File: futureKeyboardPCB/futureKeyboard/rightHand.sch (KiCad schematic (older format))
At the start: 50 parts, among them J1 Conn_01x01, J2 Conn_01x04, J3 Conn_01x01, J4 Conn_01x01, J5 Conn_01x04, J6 Conn_01x06, J7 Conn_01x06, J8 Conn_01x01, P1 CONN_01X02, P2 CONN_01X06, Q1 2SC1815, Q2 2SC1815, Q3 2SC1815, SW1 SW_SPDT, SW2 SW_Push, SW3 SW_Push, SW4 SW_Push, SW5 SW_Push, SW6 SW_Push, SW7 SW_Push, SW8 SW_Push, U1 AMS1117-1.5, U2 ESP32

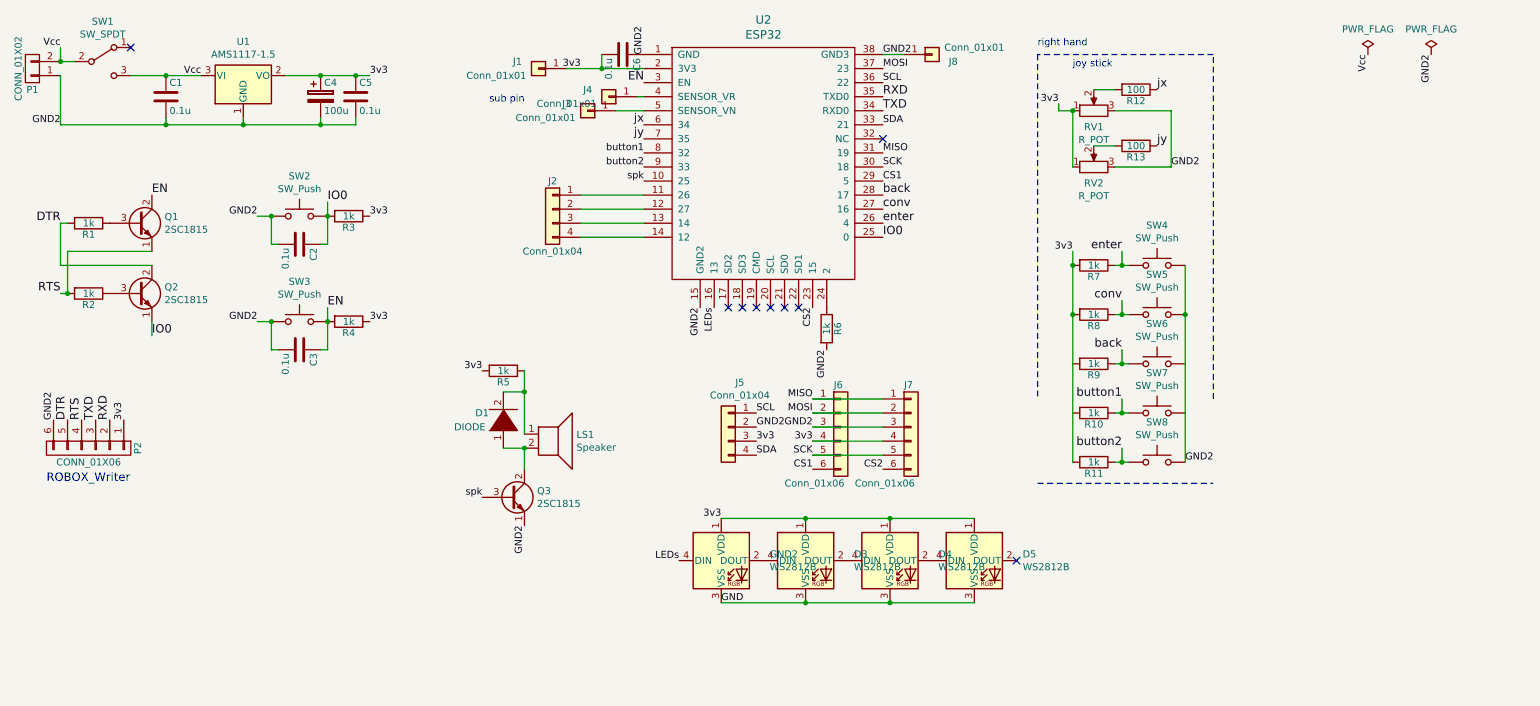
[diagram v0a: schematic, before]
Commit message: divide layors, make footprints, aligned footprints
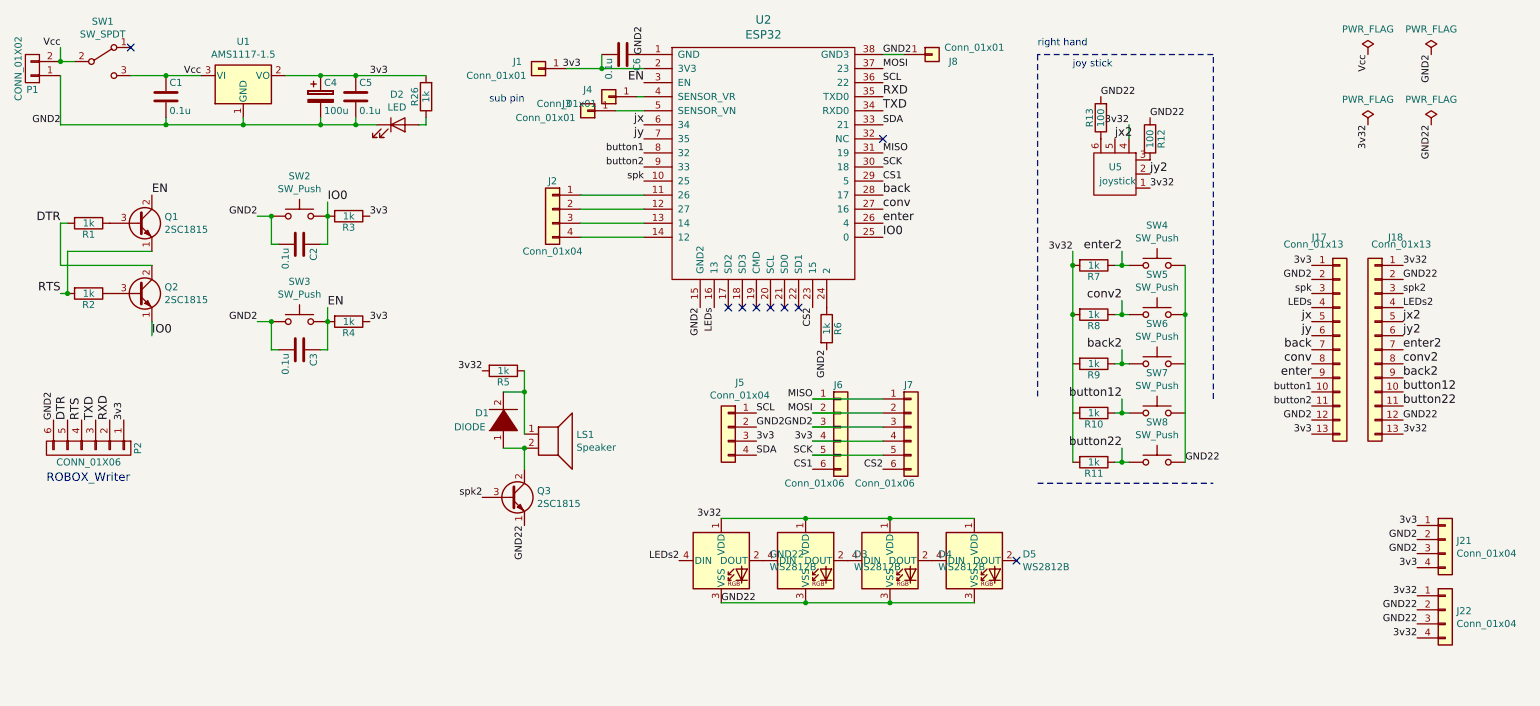
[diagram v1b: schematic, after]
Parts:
- removed RV1, RV2: R_POT, akizukit:S_POT_SMD, symbol Device:R_POT
- added D2: LED, akizukit:2012LED, symbol Device:LED
- added J17, J18: Conn_01x13, Connector_PinHeader_2.54mm:PinHeader_1x13_P2.54mm_Vertical_SMD_Pin1Left, symbol Connector_Generic:Conn_01x13
- added J21, J22: Conn_01x04, Connector_PinHeader_2.54mm:PinHeader_1x04_P2.54mm_Vertical_SMD_Pin1Left, symbol Connector_Generic:Conn_01x04
- added R26: 1k, akizukit:SMD-1608, symbol Hyper_Board_Traser-rescue:R
- added U5: joystick, akizukit:joyStick, symbol akizukit:joystick
- D3, D4, D5: footprint LED_SMD:LED_WS2812B_PLCC4_5.0x5.0mm_P3.2mm -> akizukit:WS2812B
- GND22: renamed from GND2; footprint LED_SMD:LED_WS2812B_PLCC4_5.0x5.0mm_P3.2mm -> akizukit:WS2812B
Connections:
- net GND is gone; now on net GND22: D3.3 (VSS), D4.3 (VSS), D5.3 (VSS), GND22.3 (VSS)
- net 3v3: now also J17.1 (Pin_1), J17.13 (Pin_13), J21.1 (Pin_1), J21.4 (Pin_4), R26.2; no longer D3.1 (VDD), D4.1 (VDD), D5.1 (VDD), GND22.1 (VDD), R10.2, R11.2, R5.2, R7.2, R8.2, R9.2
- net GND2: now also D2.1 (K), J17.12 (Pin_12), J17.2 (Pin_2), J21.2 (Pin_2), J21.3 (Pin_3); no longer Q3.1 (E), SW4.2, SW5.2, SW6.2, SW7.2, SW8.2
- net LEDs: now also J17.4 (Pin_4); no longer GND22.4 (DIN)
- net back: now also J17.7 (Pin_7); no longer R9.1, SW6.1
- net button1: now also J17.10 (Pin_10); no longer R10.1, SW7.1
- net button2: now also J17.11 (Pin_11); no longer R11.1, SW8.1
- net conv: now also J17.8 (Pin_8); no longer R8.1, SW5.1
- net enter: now also J17.9 (Pin_9); no longer R7.1, SW4.1
- net jx: now also J17.5 (Pin_5); no longer R12.1
- net jy: now also J17.6 (Pin_6); no longer R13.1
- net spk: now also J17.3 (Pin_3); no longer Q3.3 (B)
- net GND22: now reaches R13.2
- net GND22: now also Q3.1 (E), R12.1, SW4.2, SW5.2, SW6.2, SW7.2, SW8.2, J18.12 (Pin_12), J18.2 (Pin_2), J22.2 (Pin_2), J22.3 (Pin_3)
- net at R12.2: now also U5.3
- new net: R13.1, U5.6
- new net: D2.2 (A), R26.1
- new net 3v32: D3.1 (VDD), D4.1 (VDD), D5.1 (VDD), GND22.1 (VDD), J18.1 (Pin_1), J18.13 (Pin_13), J22.1 (Pin_1), J22.4 (Pin_4), R10.2, R11.2, R5.2, R7.2, R8.2, R9.2, U5.1, U5.4
- new net LEDs2: GND22.4 (DIN), J18.4 (Pin_4)
- new net back2: J18.9 (Pin_9), R9.1, SW6.1
- new net button12: J18.10 (Pin_10), R10.1, SW7.1
- new net button22: J18.11 (Pin_11), R11.1, SW8.1
- new net conv2: J18.8 (Pin_8), R8.1, SW5.1
- new net enter2: J18.7 (Pin_7), R7.1, SW4.1
- new net jx2: J18.5 (Pin_5), U5.5
- new net jy2: J18.6 (Pin_6), U5.2
- new net spk2: J18.3 (Pin_3), Q3.3 (B)
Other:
- moved on the sheet: R12

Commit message: change layer connecter to be same pins total
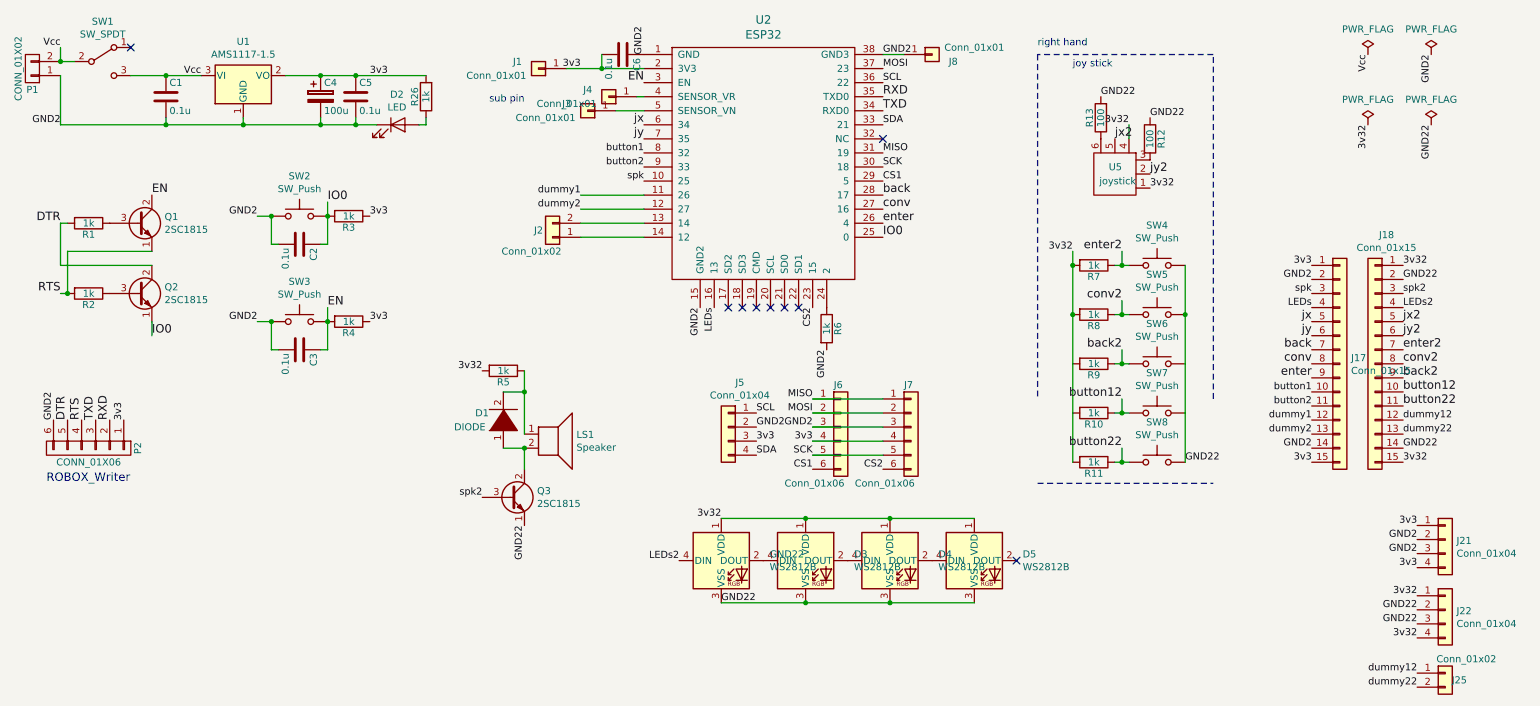
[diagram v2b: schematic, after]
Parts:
- removed J17, J18: Conn_01x13, Connector_PinHeader_2.54mm:PinHeader_1x13_P2.54mm_Vertical_SMD_Pin1Left, symbol Connector_Generic:Conn_01x13
- removed J2: Conn_01x04, Connector_PinHeader_2.54mm:PinHeader_1x04_P2.54mm_Vertical, symbol Connector_Generic:Conn_01x04
- added J17, J18: Conn_01x15, Connector_PinHeader_2.54mm:PinHeader_1x15_P2.54mm_Vertical_SMD_Pin1Left, symbol Connector_Generic:Conn_01x15
- added J2, J25: Conn_01x02, Connector_PinHeader_2.54mm:PinHeader_1x02_P2.54mm_Vertical, symbol Connector_Generic:Conn_01x02
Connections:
- net 3v3: now also J17.1 (Pin_1), J17.15 (Pin_15)
- net 3v32: now also J18.1 (Pin_1), J18.15 (Pin_15)
- net GND2: now also J17.14 (Pin_14), J17.2 (Pin_2)
- net GND22: now also J18.14 (Pin_14), J18.2 (Pin_2)
- net LEDs: now also J17.4 (Pin_4)
- net LEDs2: now also J18.4 (Pin_4)
- net back: now also J17.7 (Pin_7)
- net back2: now also J18.9 (Pin_9)
- net button1: now also J17.10 (Pin_10)
- net button12: now also J18.10 (Pin_10)
- net button2: now also J17.11 (Pin_11)
- net button22: now also J18.11 (Pin_11)
- net conv: now also J17.8 (Pin_8)
- net conv2: now also J18.8 (Pin_8)
- net enter: now also J17.9 (Pin_9)
- net enter2: now also J18.7 (Pin_7)
- net jx: now also J17.5 (Pin_5)
- net jx2: now also J18.5 (Pin_5)
- net jy: now also J17.6 (Pin_6)
- net jy2: now also J18.6 (Pin_6)
- net spk: now also J17.3 (Pin_3)
- net spk2: now also J18.3 (Pin_3)
- net dummy1: now reaches U2.11 (26)
- net dummy1: now also J17.12 (Pin_12)
- net dummy2: now reaches U2.12 (27)
- net dummy2: now also J17.13 (Pin_13)
- net at U2.13 (14): now also J2.2 (Pin_2)
- net at U2.14 (12): now also J2.1 (Pin_1)
- new net dummy12: J18.12 (Pin_12), J25.1 (Pin_1)
- new net dummy22: J18.13 (Pin_13), J25.2 (Pin_2)
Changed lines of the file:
@@
 Text Label 6050 3700 0    50   ~ 0
 3v3
-$Comp
-L Connector_Generic:Conn_01x04 J2
-U 1 1 5F672161
-P 4600 2050
-F 0 "J2" H 4600 2250 50  0000 C CNN
-F 1 "Conn_01x04" H 4600 1750 50  0000 C CNN
-F 2 "Connector_PinHeader_2.54mm:PinHeader_1x04_P2.54mm_Vertical" H 4600 2050 50  0001 C CNN
-F 3 "~" H 4600 2050 50  0001 C CNN
-	1    4600 2050
-	-1   0    0    -1
-$EndComp
 Text Label 5250 1650 2    50   ~ 0
 button1
@@
 Text Label 10000 2550 2    50   ~ 0
 GND2
-Text Label 10650 3650 0    50   ~ 0
-3v32
-Text Label 10650 3550 0    50   ~ 0
-GND22
-Text Label 10000 3550 2    50   ~ 0
+Text Label 10650 3850 0    50   ~ 0
+3v32
+Text Label 10650 3750 0    50   ~ 0
+GND22
+Text Label 10000 3750 2    50   ~ 0
 GND2
-Text Label 10000 3650 2    50   ~ 0
-3v3
-$Comp
-L Connector_Generic:Conn_01x13 J17
-U 1 1 5F93E5DF
-P 10200 3050
-F 0 "J17" H 10000 3850 50  0000 L CNN
-F 1 "Conn_01x13" H 9800 3800 50  0000 L CNN
-F 2 "Connector_PinHeader_2.54mm:PinHeader_1x13_P2.54mm_Vertical_SMD_Pin1Left" H 10200 3050 50  0001 C CNN
-F 3 "~" H 10200 3050 50  0001 C CNN
-	1    10200 3050
-	1    0    0    -1
-$EndComp
-$Comp
-L Connector_Generic:Conn_01x13 J18
-U 1 1 5F941DEC
-P 10450 3050
-F 0 "J18" H 10250 3850 50  0000 L CNN
-F 1 "Conn_01x13" H 10050 3800 50  0000 L CNN
-F 2 "Connector_PinHeader_2.54mm:PinHeader_1x13_P2.54mm_Vertical_SMD_Pin1Left" H 10450 3050 50  0001 C CNN
-F 3 "~" H 10450 3050 50  0001 C CNN
-	1    10450 3050
-	-1   0    0    -1
-$EndComp
+Text Label 10000 3850 2    50   ~ 0
+3v3
 Text Label 10850 1450 3    50   ~ 0
 GND22
@@
 Text Label 10750 4500 2    50   ~ 0
 GND2
+$Comp
+L Connector_Generic:Conn_01x02 J2
+U 1 1 5FA72512
+P 4600 2250
+F 0 "J2" H 4700 2200 50  0000 C CNN
+F 1 "Conn_01x02" H 4750 2350 50  0000 C CNN
+F 2 "Connector_PinHeader_2.54mm:PinHeader_1x02_P2.54mm_Vertical" H 4600 2250 50  0001 C CNN
+F 3 "~" H 4600 2250 50  0001 C CNN
+	1    4600 2250
+	-1   0    0    1
+$EndComp
+Text Label 4800 2050 2    50   ~ 0
+dummy2
+Text Label 4800 1950 2    50   ~ 0
+dummy1
+Text Label 10000 3650 2    50   ~ 0
+dummy2
+Text Label 10000 3550 2    50   ~ 0
+dummy1
+Text Label 10650 3650 0    50   ~ 0
+dummy22
+Text Label 10650 3550 0    50   ~ 0
+dummy12
+$Comp
+L Connector_Generic:Conn_01x15 J17
+U 1 1 5FA83732
+P 10200 3150
+F 0 "J17" H 10280 3192 50  0000 L CNN
+F 1 "Conn_01x15" H 10280 3101 50  0000 L CNN
+F 2 "Connector_PinHeader_2.54mm:PinHeader_1x15_P2.54mm_Vertical_SMD_Pin1Left" H 10200 3150 50  0001 C CNN
+F 3 "~" H 10200 3150 50  0001 C CNN
+	1    10200 3150
+	1    0    0    -1
+$EndComp
+$Comp
+L Connector_Generic:Conn_01x15 J18
+U 1 1 5FA84614
+P 10450 3150
+F 0 "J18" H 10368 4067 50  0000 C CNN
+F 1 "Conn_01x15" H 10368 3976 50  0000 C CNN
+F 2 "Connector_PinHeader_2.54mm:PinHeader_1x15_P2.54mm_Vertical_SMD_Pin1Left" H 10450 3150 50  0001 C CNN
+F 3 "~" H 10450 3150 50  0001 C CNN
+	1    10450 3150
+	-1   0    0    -1
+$EndComp
+$Comp
+L Connector_Generic:Conn_01x02 J25
+U 1 1 5FA85470
+P 10950 5350
+F 0 "J25" H 11050 5300 50  0000 C CNN
+F 1 "Conn_01x02" H 11100 5450 50  0000 C CNN
+F 2 "Connector_PinHeader_2.54mm:PinHeader_1x02_P2.54mm_Vertical" H 10950 5350 50  0001 C CNN
+F 3 "~" H 10950 5350 50  0001 C CNN
+	1    10950 5350
+	1    0    0    -1
+$EndComp
+Text Label 10750 5450 2    50   ~ 0
+dummy22
+Text Label 10750 5350 2    50   ~ 0
+dummy12
 $EndSCHEMATC

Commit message: fix circuit bags, and placement electric parts
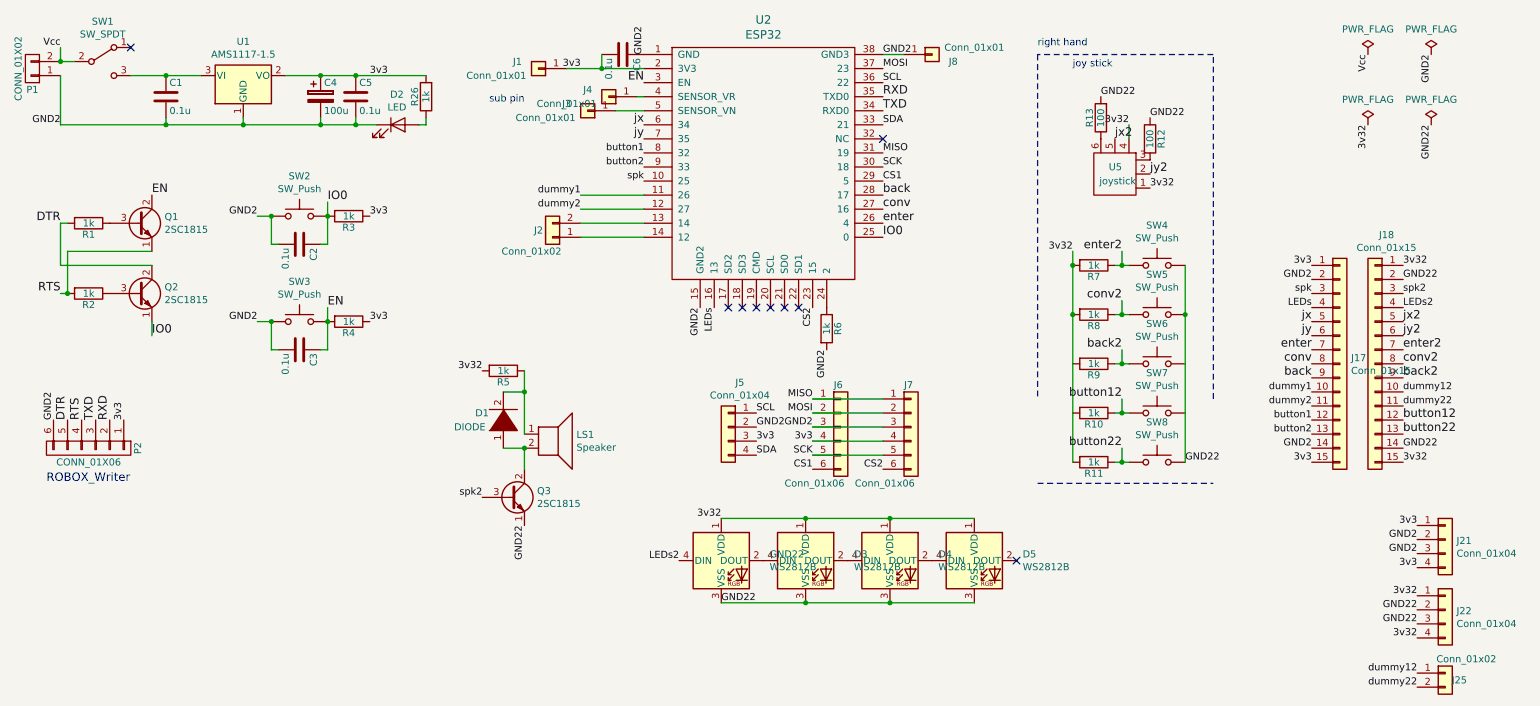
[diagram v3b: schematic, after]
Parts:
- removed U1: AMS1117-1.5, akizukit:AZ1086H, symbol Regulator_Linear:AMS1117-1.5
- added U1: AMS1117-1.5, Package_TO_SOT_SMD:SOT-223-3_TabPin2, symbol ume-boshi:AMS1117-1.5
- P2: footprint Connector_PinHeader_2.54mm:PinHeader_1x06_P2.54mm_Vertical -> Connector_PinHeader_2.54mm:PinHeader_1x06_P2.54mm_Horizontal
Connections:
- net 3v3: now also U1.2 (VO)
- net GND2: now also U1.1 (GND)
- net Vcc: no longer C1.1, SW1.3 (C)
- net back: now also J17.9 (Pin_9); no longer J17.7 (Pin_7)
- net button1: now also J17.12 (Pin_12); no longer J17.10 (Pin_10)
- net button12: now also J18.12 (Pin_12); no longer J18.10 (Pin_10)
- net button2: now also J17.13 (Pin_13); no longer J17.11 (Pin_11)
- net button22: now also J18.13 (Pin_13); no longer J18.11 (Pin_11)
- net dummy1: now also J17.10 (Pin_10); no longer J17.12 (Pin_12)
- net dummy12: now also J18.10 (Pin_10); no longer J18.12 (Pin_12)
- net dummy2: now also J17.11 (Pin_11); no longer J17.13 (Pin_13)
- net dummy22: now also J18.11 (Pin_11); no longer J18.13 (Pin_13)
- net enter: now also J17.7 (Pin_7); no longer J17.9 (Pin_9)
- new net: C1.1, SW1.3 (C), U1.3 (VI)
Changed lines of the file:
@@
 	2950 1100 3200 1100
 Connection ~ 3200 1100
-$Comp
-L Regulator_Linear:AMS1117-1.5 U?
-U 1 1 5F58975C
-P 2400 1100
-AR Path="/5F58975C" Ref="U?"  Part="1"
-AR Path="/5F548958/5F58975C" Ref="U1"  Part="1"
-F 0 "U1" H 2400 1342 50  0000 C CNN
-F 1 "AMS1117-1.5" H 2400 1251 50  0000 C CNN
-F 2 "akizukit:AZ1086H" H 2400 1300 50  0001 C CNN
-F 3 "http://www.advanced-monolithic.com/pdf/ds1117.pdf" H 2500 850 50  0001 C CNN
-	1    2400 1100
-	1    0    0    -1
-$EndComp
 Wire Wire Line
 	1850 1100 2100 1100
@@
 F 0 "P2" H 1300 4100 50  0000 C CNN
 F 1 "CONN_01X06" V 1400 3750 50  0000 C CNN
-F 2 "Connector_PinHeader_2.54mm:PinHeader_1x06_P2.54mm_Vertical" H 1300 3750 50  0001 C CNN
+F 2 "Connector_PinHeader_2.54mm:PinHeader_1x06_P2.54mm_Horizontal" H 1300 3750 50  0001 C CNN
 F 3 "" H 1300 3750 50  0000 C CNN
 	1    1300 3750
@@
 Text Label 3300 1100 0    50   ~ 0
 3v3
-Text Label 1100 900  2    50   ~ 0
-Vcc
 Text Label 10400 950  3    50   ~ 0
 Vcc
@@
 Wire Wire Line
 	1100 1100 1100 1450
-Wire Wire Line
-	1100 900  1100 1000
-Connection ~ 1100 1000
 Text Label 3300 2100 0    50   ~ 0
 3v3
@@
 Text Label 9100 3850 0    50   ~ 0
 GND22
-Text Label 2100 1100 2    50   ~ 0
-Vcc
 Wire Wire Line
 	7100 950  6950 950
@@
 Text Label 10650 2950 0    60   ~ 0
 jy2
-Text Label 10650 3050 0    60   ~ 0
-enter2
 Text Label 10650 3150 0    60   ~ 0
 conv2
 Text Label 10650 3250 0    60   ~ 0
 back2
-Text Label 10650 3350 0    60   ~ 0
+Text Label 10650 3550 0    60   ~ 0
 button12
-Text Label 10650 3450 0    60   ~ 0
-button22
 Text Label 10000 2850 2    60   ~ 0
 jx
@@
 Text Label 10000 2650 2    50   ~ 0
 spk
-Text Label 10000 3350 2    50   ~ 0
+Text Label 10000 3550 2    50   ~ 0
 button1
-Text Label 10000 3450 2    50   ~ 0
+Text Label 10000 3650 2    50   ~ 0
 button2
 Text Label 10000 2750 2    50   ~ 0
 LEDs
-Text Label 10000 3050 2    60   ~ 0
+Text Label 10000 3250 2    60   ~ 0
 back
 Text Label 10000 3150 2    60   ~ 0
 conv
-Text Label 10000 3250 2    60   ~ 0
+Text Label 10000 3050 2    60   ~ 0
 enter
 Text Label 10000 2450 2    50   ~ 0
@@
 Text Label 4800 1950 2    50   ~ 0
 dummy1
-Text Label 10000 3650 2    50   ~ 0
+Text Label 10000 3450 2    50   ~ 0
 dummy2
-Text Label 10000 3550 2    50   ~ 0
+Text Label 10000 3350 2    50   ~ 0
 dummy1
-Text Label 10650 3650 0    50   ~ 0
+Text Label 10650 3450 0    50   ~ 0
 dummy22
-Text Label 10650 3550 0    50   ~ 0
+Text Label 10650 3350 0    50   ~ 0
 dummy12
 $Comp
@@
 Text Label 10750 5350 2    50   ~ 0
 dummy12
+Text Label 10650 3050 0    60   ~ 0
+enter2
+Connection ~ 1100 1000
+Wire Wire Line
+	1100 900  1100 1000
+Text Label 1100 900  2    50   ~ 0
+Vcc
+Text Label 10650 3650 0    60   ~ 0
+button22
+$Comp
+L ume-boshi:AMS1117-1.5 U?
+U 1 1 5F5EE260
+P 2400 1100
+AR Path="/5F548F89/5F5EE260" Ref="U?"  Part="1"
+AR Path="/5F548958/5F5EE260" Ref="U1"  Part="1"
+F 0 "U1" H 2400 1342 50  0000 C CNN
+F 1 "AMS1117-1.5" H 2400 1251 50  0000 C CNN
+F 2 "Package_TO_SOT_SMD:SOT-223-3_TabPin2" H 2400 1300 50  0001 C CNN
+F 3 "http://www.advanced-monolithic.com/pdf/ds1117.pdf" H 2500 850 50  0001 C CNN
+	1    2400 1100
+	1    0    0    -1
+$EndComp
 $EndSCHEMATC
